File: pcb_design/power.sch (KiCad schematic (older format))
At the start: 35 parts, among them Q1 BSC340N08, U11 LM3488, U13 LM1117IMP-v.v, U9 LM22676QTJ-5.0

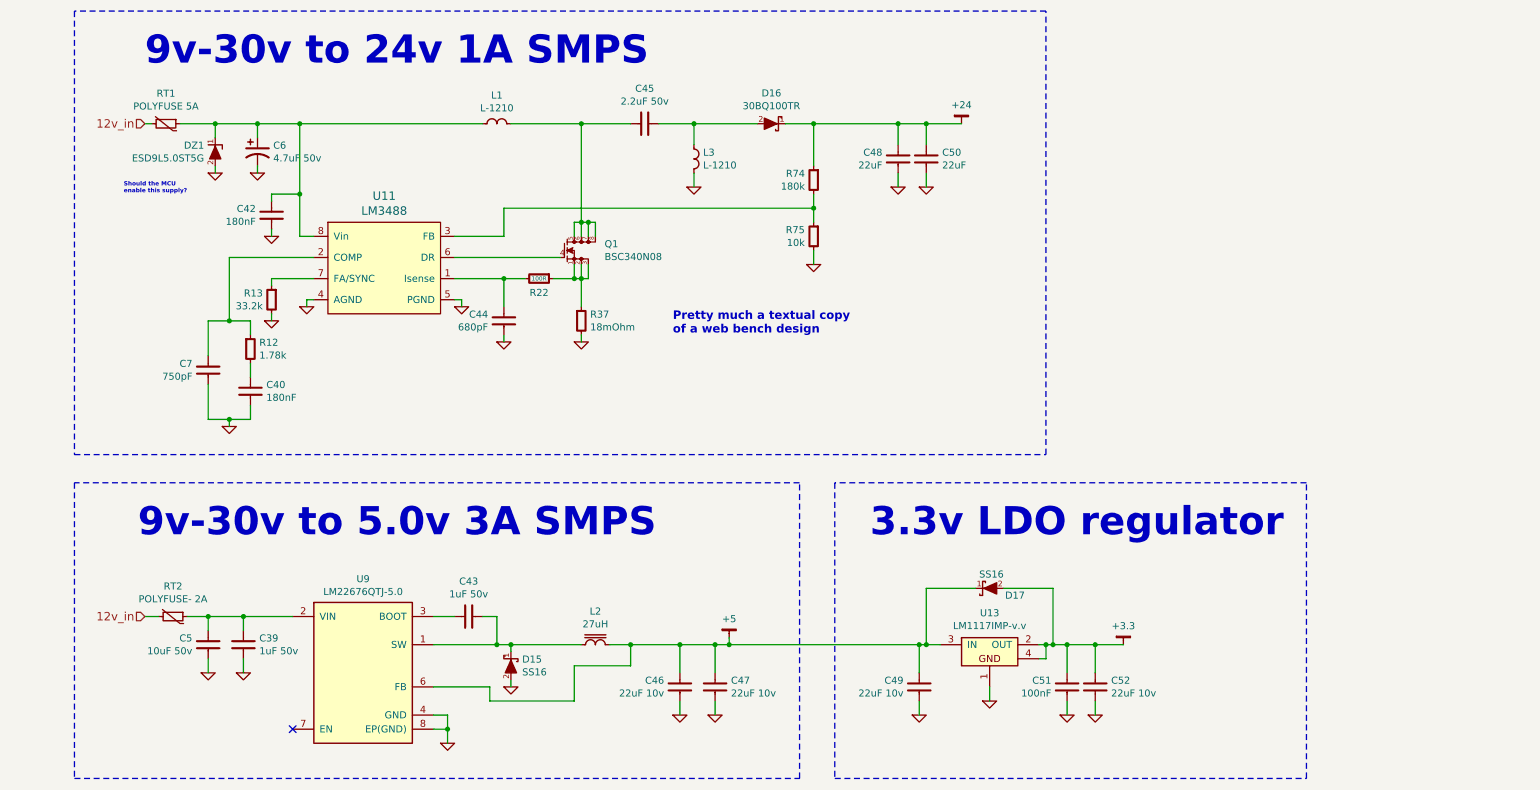
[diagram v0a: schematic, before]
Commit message: Resolver routed using push pull buffer
Signed-off-by: Marcos Chaparro <mchaparro@paltatech.com>
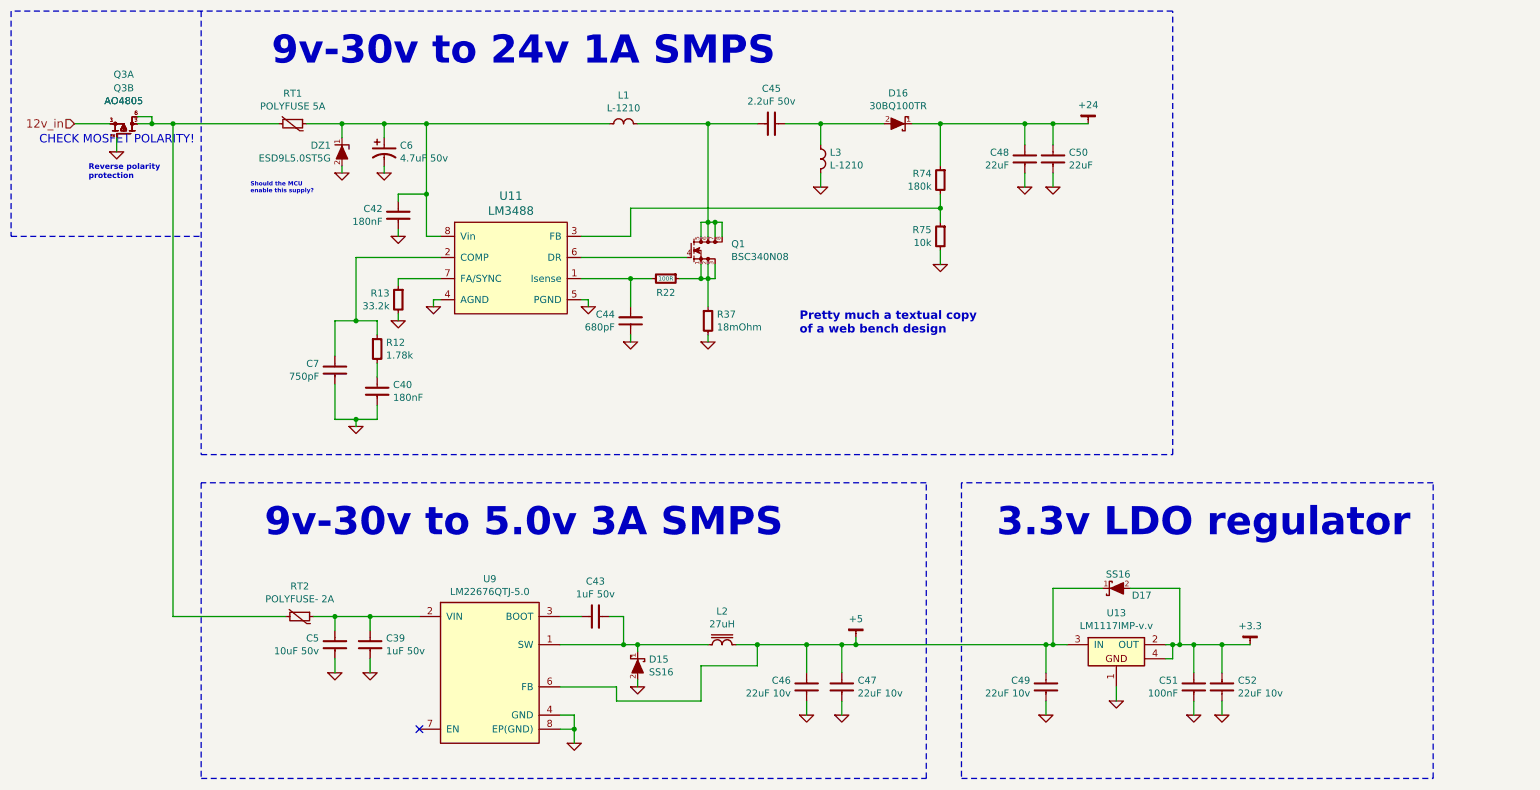
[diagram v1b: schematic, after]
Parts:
- added Q3: AO4805, IPC7351-Nominal:SOIC127P600X175-8, symbol AO4805
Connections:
- net 12v_in: now also Q3.1 (S2), Q3.3 (S1); no longer RT1.2, RT2.2
- net GND: now also Q3.2 (G1), Q3.4 (G1)
- new net: Q3.5 (D1A), Q3.6 (D1B), Q3.7 (D2A), Q3.8 (D2B), RT1.2, RT2.2
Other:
- note added: "CHECK MOSFET POLARITY!"
- note added: "Reverse polarity\nprotection"
- moved on the sheet: C39, C40, C42, C43, C44, C45, C46, C47, C48, C49, C5, C50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

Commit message: Routing complete. Added 3D models. No DRC errors, a few ERC warnings
Signed-off-by: Marcos Chaparro <mchaparro@paltatech.com>
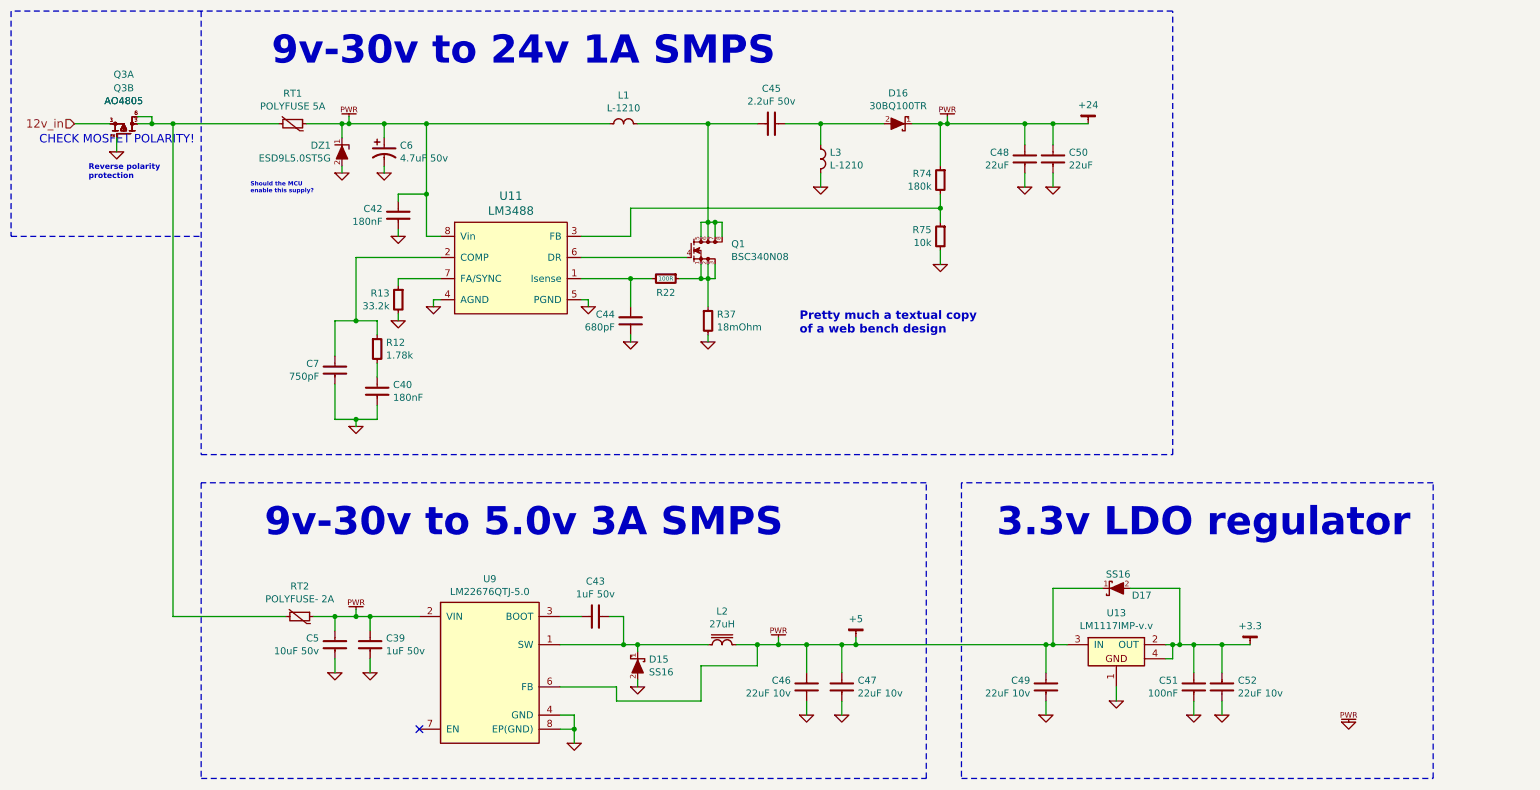
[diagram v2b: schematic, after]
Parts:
- L2: footprint manuf:BOURNS-SRP1238A -> manuf:BOURNS-SDR1307
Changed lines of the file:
@@
 Connection ~ 3000 4150
 $Comp
-L GND #PWR067
+L GND #PWR073
 U 1 1 588BC982
 P 3000 4200
-F 0 "#PWR067" H 3000 4200 30  0001 C CNN
+F 0 "#PWR073" H 3000 4200 30  0001 C CNN
 F 1 "GND" H 3000 4130 30  0001 C CNN
 F 2 "" H 3000 4200 60  0000 C CNN
@@
 	3300 3150 3300 3200
 $Comp
-L GND #PWR068
+L GND #PWR074
 U 1 1 588BD2D9
 P 3300 3450
-F 0 "#PWR068" H 3300 3450 30  0001 C CNN
+F 0 "#PWR074" H 3300 3450 30  0001 C CNN
 F 1 "GND" H 3300 3380 30  0001 C CNN
 F 2 "" H 3300 3450 60  0000 C CNN
@@
 	3300 3450 3300 3400
 $Comp
-L GND #PWR069
+L GND #PWR075
 U 1 1 588BD345
 P 3550 3350
-F 0 "#PWR069" H 3550 3350 30  0001 C CNN
+F 0 "#PWR075" H 3550 3350 30  0001 C CNN
 F 1 "GND" H 3550 3280 30  0001 C CNN
 F 2 "" H 3550 3350 60  0000 C CNN
@@
 	4650 3300 4650 3350
 $Comp
-L GND #PWR070
+L GND #PWR076
 U 1 1 588BD634
 P 4650 3350
-F 0 "#PWR070" H 4650 3350 30  0001 C CNN
+F 0 "#PWR076" H 4650 3350 30  0001 C CNN
 F 1 "GND" H 4650 3280 30  0001 C CNN
 F 2 "" H 4650 3350 60  0000 C CNN
@@
 	4950 3550 4950 3600
 $Comp
-L GND #PWR071
+L GND #PWR077
 U 1 1 588BDA1B
 P 4950 3600
-F 0 "#PWR071" H 4950 3600 30  0001 C CNN
+F 0 "#PWR077" H 4950 3600 30  0001 C CNN
 F 1 "GND" H 4950 3530 30  0001 C CNN
 F 2 "" H 4950 3600 60  0000 C CNN
@@
 	5500 3550 5500 3600
 $Comp
-L GND #PWR072
+L GND #PWR078
 U 1 1 588BDE06
 P 5500 3600
-F 0 "#PWR072" H 5500 3600 30  0001 C CNN
+F 0 "#PWR078" H 5500 3600 30  0001 C CNN
 F 1 "GND" H 5500 3530 30  0001 C CNN
 F 2 "" H 5500 3600 60  0000 C CNN
@@
 Connection ~ 3500 2550
 $Comp
-L GND #PWR073
+L GND #PWR079
 U 1 1 588BFA6D
 P 3300 2850
-F 0 "#PWR073" H 3300 2850 30  0001 C CNN
+F 0 "#PWR079" H 3300 2850 30  0001 C CNN
 F 1 "GND" H 3300 2780 30  0001 C CNN
 F 2 "" H 3300 2850 60  0000 C CNN
@@
 	3200 2150 3200 2050
 $Comp
-L GND #PWR074
+L GND #PWR080
 U 1 1 588C0261
 P 3200 2400
-F 0 "#PWR074" H 3200 2400 30  0001 C CNN
+F 0 "#PWR080" H 3200 2400 30  0001 C CNN
 F 1 "GND" H 3200 2330 30  0001 C CNN
 F 2 "" H 3200 2400 60  0000 C CNN
@@
 	6050 2050 6750 2050
 $Comp
-L GND #PWR075
+L GND #PWR081
 U 1 1 588C0D64
 P 6300 2500
-F 0 "#PWR075" H 6300 2500 30  0001 C CNN
+F 0 "#PWR081" H 6300 2500 30  0001 C CNN
 F 1 "GND" H 6300 2430 30  0001 C CNN
 F 2 "" H 6300 2500 60  0000 C CNN
@@
 	6950 2050 8200 2050
 $Comp
-L GND #PWR076
+L GND #PWR082
 U 1 1 588C18FD
 P 7150 3050
-F 0 "#PWR076" H 7150 3050 30  0001 C CNN
+F 0 "#PWR082" H 7150 3050 30  0001 C CNN
 F 1 "GND" H 7150 2980 30  0001 C CNN
 F 2 "" H 7150 3050 60  0000 C CNN
@@
 Connection ~ 7750 2050
 $Comp
-L GND #PWR077
+L GND #PWR083
 U 1 1 588C2312
 P 7750 2500
-F 0 "#PWR077" H 7750 2500 30  0001 C CNN
+F 0 "#PWR083" H 7750 2500 30  0001 C CNN
 F 1 "GND" H 7750 2430 30  0001 C CNN
 F 2 "" H 7750 2500 60  0000 C CNN
@@
 	7750 2500 7750 2400
 $Comp
-L GND #PWR078
+L GND #PWR084
 U 1 1 588C2433
 P 7950 2500
-F 0 "#PWR078" H 7950 2500 30  0001 C CNN
+F 0 "#PWR084" H 7950 2500 30  0001 C CNN
 F 1 "GND" H 7950 2430 30  0001 C CNN
 F 2 "" H 7950 2500 60  0000 C CNN
@@
 Connection ~ 3100 5550
 $Comp
-L GND #PWR079
+L GND #PWR085
 U 1 1 588C4382
 P 2850 5950
-F 0 "#PWR079" H 2850 5950 30  0001 C CNN
+F 0 "#PWR085" H 2850 5950 30  0001 C CNN
 F 1 "GND" H 2850 5880 30  0001 C CNN
 F 2 "" H 2850 5950 60  0000 C CNN
@@
 	2850 5950 2850 5850
 $Comp
-L GND #PWR080
+L GND #PWR086
 U 1 1 588C4468
 P 3100 5950
-F 0 "#PWR080" H 3100 5950 30  0001 C CNN
+F 0 "#PWR086" H 3100 5950 30  0001 C CNN
 F 1 "GND" H 3100 5880 30  0001 C CNN
 F 2 "" H 3100 5950 60  0000 C CNN
@@
 Connection ~ 4900 5750
 $Comp
-L GND #PWR081
+L GND #PWR087
 U 1 1 588C56F7
 P 5000 6050
-F 0 "#PWR081" H 5000 6050 30  0001 C CNN
+F 0 "#PWR087" H 5000 6050 30  0001 C CNN
 F 1 "GND" H 5000 5980 30  0001 C CNN
 F 2 "" H 5000 6050 60  0000 C CNN
@@
 F 0 "L2" V 5363 5750 50  0000 C CNN
 F 1 "27uH" V 5454 5750 50  0000 C CNN
-F 2 "manuf:BOURNS-SRP1238A" H 5600 5800 60  0001 C CNN
+F 2 "manuf:BOURNS-SDR1307" H 5600 5800 60  0001 C CNN
 F 3 "" H 5600 5800 60  0000 C CNN
 F 4 "SDR1307-270ML" H 5600 5750 60  0001 C CNN "mfg#"
@@
 Connection ~ 6200 5750
 $Comp
-L GND #PWR082
+L GND #PWR088
 U 1 1 588C63EB
 P 6200 6250
-F 0 "#PWR082" H 6200 6250 30  0001 C CNN
+F 0 "#PWR088" H 6200 6250 30  0001 C CNN
 F 1 "GND" H 6200 6180 30  0001 C CNN
 F 2 "" H 6200 6250 60  0000 C CNN
@@
 $EndComp
 $Comp
-L GND #PWR083
+L GND #PWR089
 U 1 1 588C6447
 P 6450 6250
-F 0 "#PWR083" H 6450 6250 30  0001 C CNN
+F 0 "#PWR089" H 6450 6250 30  0001 C CNN
 F 1 "GND" H 6450 6180 30  0001 C CNN
 F 2 "" H 6450 6250 60  0000 C CNN
@@
 NoConn ~ 3450 6350
 $Comp
-L GND #PWR084
+L GND #PWR090
 U 1 1 588C6DC2
 P 4550 6450
-F 0 "#PWR084" H 4550 6450 30  0001 C CNN
+F 0 "#PWR090" H 4550 6450 30  0001 C CNN
 F 1 "GND" H 4550 6380 30  0001 C CNN
 F 2 "" H 4550 6450 60  0000 C CNN
@@
 Connection ~ 7900 5750
 $Comp
-L GND #PWR085
+L GND #PWR091
 U 1 1 588C792B
 P 7900 6250
-F 0 "#PWR085" H 7900 6250 30  0001 C CNN
+F 0 "#PWR091" H 7900 6250 30  0001 C CNN
 F 1 "GND" H 7900 6180 30  0001 C CNN
 F 2 "" H 7900 6250 60  0000 C CNN
@@
 	7900 6250 7900 6150
 $Comp
-L GND #PWR086
+L GND #PWR092
 U 1 1 588C79EC
 P 8400 6150
-F 0 "#PWR086" H 8400 6150 30  0001 C CNN
+F 0 "#PWR092" H 8400 6150 30  0001 C CNN
 F 1 "GND" H 8400 6080 30  0001 C CNN
 F 2 "" H 8400 6150 60  0000 C CNN
@@
 Connection ~ 8950 5750
 $Comp
-L GND #PWR087
+L GND #PWR093
 U 1 1 588C813C
 P 8950 6250
-F 0 "#PWR087" H 8950 6250 30  0001 C CNN
+F 0 "#PWR093" H 8950 6250 30  0001 C CNN
 F 1 "GND" H 8950 6180 30  0001 C CNN
 F 2 "" H 8950 6250 60  0000 C CNN
@@
 	8950 6250 8950 6150
 $Comp
-L GND #PWR088
+L GND #PWR094
 U 1 1 588C81BF
 P 9150 6250
-F 0 "#PWR088" H 9150 6250 30  0001 C CNN
+F 0 "#PWR094" H 9150 6250 30  0001 C CNN
 F 1 "GND" H 9150 6180 30  0001 C CNN
 F 2 "" H 9150 6250 60  0000 C CNN
@@
 	10650 4600 7300 4600
 $Comp
-L +3.3 #PWR089
+L +3.3 #PWR095
 U 1 1 588BD2B2
 P 9350 5750
-F 0 "#PWR089" H 9400 5800 30  0001 C CNN
+F 0 "#PWR095" H 9400 5800 30  0001 C CNN
 F 1 "+3.3" H 9350 5883 50  0000 C CNN
 F 2 "" H 800 0   60  0000 C CNN
@@
 $EndComp
 $Comp
-L +5 #PWR090
+L +5 #PWR096
 U 1 1 588BD705
 P 6550 5700
-F 0 "#PWR090" H 6600 5750 30  0001 C CNN
+F 0 "#PWR096" H 6600 5750 30  0001 C CNN
 F 1 "+5" H 6550 5833 50  0000 C CNN
 F 2 "" H 500 50  60  0000 C CNN
@@
 Connection ~ 2900 2050
 $Comp
-L GND #PWR091
+L GND #PWR097
 U 1 1 588CB9A0
 P 2900 2400
-F 0 "#PWR091" H 2900 2400 30  0001 C CNN
+F 0 "#PWR097" H 2900 2400 30  0001 C CNN
 F 1 "GND" H 2900 2330 30  0001 C CNN
 F 2 "" H 2900 2400 60  0000 C CNN
@@
 Connection ~ 7950 5750
 $Comp
-L +24 #PWR092
+L +24 #PWR098
 U 1 1 588CFB19
 P 8200 2050
-F 0 "#PWR092" H 800 50  30  0001 C CNN
+F 0 "#PWR098" H 800 50  30  0001 C CNN
 F 1 "+24" H 8200 2183 50  0000 C CNN
 F 2 "" H 800 0   60  0000 C CNN
@@
 Connection ~ 1550 2050
 $Comp
-L GND #PWR093
+L GND #PWR099
 U 1 1 588F9181
 P 1300 2250
-F 0 "#PWR093" H 1300 2250 30  0001 C CNN
+F 0 "#PWR099" H 1300 2250 30  0001 C CNN
 F 1 "GND" H 1300 2180 30  0001 C CNN
 F 2 "" H 1300 2250 60  0000 C CNN
@@
 Text Notes 750  2200 0    60   ~ 0
 CHECK MOSFET POLARITY!
+$Comp
+L PWR_FLAG #PWR0100
+U 1 1 58939EB5
+P 6000 5700
+F 0 "#PWR0100" H 6050 5750 50  0001 C CNN
+F 1 "PWR_FLAG" H -3050 3650 50  0001 C CNN
+F 2 "" H -3050 3650 60  0000 C CNN
+F 3 "" H -3050 3650 60  0000 C CNN
+	1    6000 5700
+	1    0    0    -1
+$EndComp
+Wire Wire Line
+	6000 5700 6000 5750
+Connection ~ 6000 5750
+$Comp
+L PWR_FLAG #PWR0101
+U 1 1 5893A517
+P 7200 2000
+F 0 "#PWR0101" H 7250 2050 50  0001 C CNN
+F 1 "PWR_FLAG" H -1850 -50 50  0001 C CNN
+F 2 "" H -1850 -50 60  0000 C CNN
+F 3 "" H -1850 -50 60  0000 C CNN
+	1    7200 2000
+	1    0    0    -1
+$EndComp
+Wire Wire Line
+	7200 2000 7200 2050
+Connection ~ 7200 2050
+$Comp
+L PWR_FLAG #PWR0102
+U 1 1 5894047A
+P 3000 5500
+F 0 "#PWR0102" H 50  150 50  0001 C CNN
+F 1 "PWR_FLAG" H 50  150 50  0001 C CNN
+F 2 "" H 50  150 60  0000 C CNN
+F 3 "" H 50  150 60  0000 C CNN
+	1    3000 5500
+	1    0    0    -1
+$EndComp
+Wire Wire Line
+	3000 5500 3000 5550
+Connection ~ 3000 5550
+$Comp
+L PWR_FLAG #PWR0103
+U 1 1 589407AF
+P 2950 2000
+F 0 "#PWR0103" H -550 50  50  0001 C CNN
+F 1 "PWR_FLAG" H -550 50  50  0001 C CNN
+F 2 "" H -550 50  60  0000 C CNN
+F 3 "" H -550 50  60  0000 C CNN
+	1    2950 2000
+	1    0    0    -1
+$EndComp
+Wire Wire Line
+	2950 2000 2950 2050
+Connection ~ 2950 2050
+$Comp
+L PWR_FLAG #PWR0104
+U 1 1 58945B82
+P 10050 6300
+F 0 "#PWR0104" H 10100 6350 50  0001 C CNN
+F 1 "PWR_FLAG" H -200 -200 50  0001 C CNN
+F 2 "" H -200 -200 60  0000 C CNN
+F 3 "" H -200 -200 60  0000 C CNN
+	1    10050 6300
+	1    0    0    -1
+$EndComp
+$Comp
+L GND #PWR0105
+U 1 1 58945C4D
+P 10050 6300
+F 0 "#PWR0105" H 10050 6300 30  0001 C CNN
+F 1 "GND" H 10050 6230 30  0001 C CNN
+F 2 "" H 10050 6300 60  0000 C CNN
+F 3 "" H 10050 6300 60  0000 C CNN
+	1    10050 6300
+	1    0    0    -1
+$EndComp
 $EndSCHEMATC

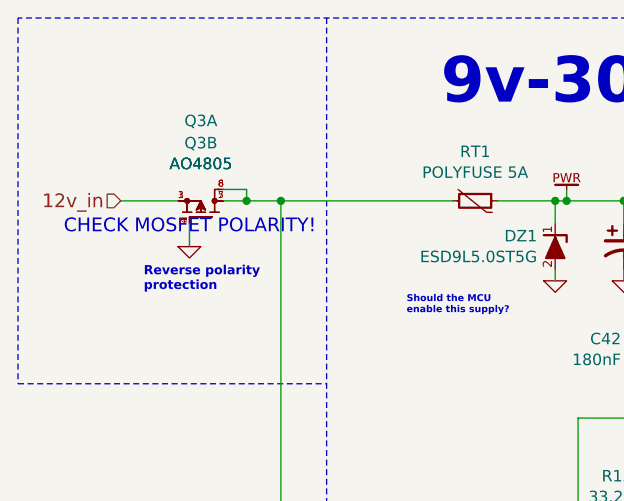
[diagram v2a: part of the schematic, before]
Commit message: Added frequency set resistors for the resolver. Fixed protection mosfet installed backwards. More 3D models
Signed-off-by: Marcos Chaparro <mchaparro@paltatech.com>
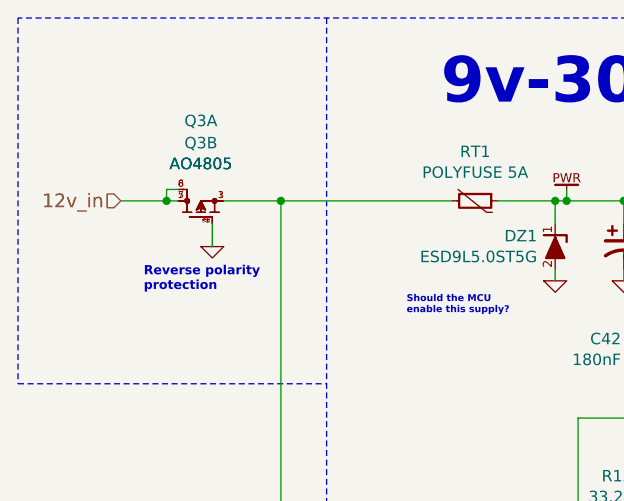
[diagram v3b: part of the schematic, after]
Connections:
- net 12v_in: now also Q3.5 (D1A), Q3.6 (D1B), Q3.7 (D2A), Q3.8 (D2B); no longer Q3.1 (S2), Q3.3 (S1)
- new net: Q3.1 (S2), Q3.3 (S1), RT1.2, RT2.2
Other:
- note removed: "CHECK MOSFET POLARITY!"
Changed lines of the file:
@@
 F 4 "PMOS AOS AO4805" H -1500 -2850 60  0001 C CNN "BOM"
 	1    1350 2100
-	0    -1   -1   0
+	0    1    -1   0
 $EndComp
 Wire Wire Line
 	1000 2050 1250 2050
-Wire Wire Line
-	1450 2000 1550 2000
-Wire Wire Line
-	1550 2000 1550 2050
-Connection ~ 1550 2050
 $Comp
 L GND #PWR099
 U 1 1 588F9181
-P 1300 2250
-F 0 "#PWR099" H 1300 2250 30  0001 C CNN
-F 1 "GND" H 1300 2180 30  0001 C CNN
-F 2 "" H 1300 2250 60  0000 C CNN
-F 3 "" H 1300 2250 60  0000 C CNN
-	1    1300 2250
+P 1400 2250
+F 0 "#PWR099" H 1400 2250 30  0001 C CNN
+F 1 "GND" H 1400 2180 30  0001 C CNN
+F 2 "" H 1400 2250 60  0000 C CNN
+F 3 "" H 1400 2250 60  0000 C CNN
+	1    1400 2250
 	1    0    0    -1
 $EndComp
 Wire Wire Line
-	1300 2250 1300 2150
+	1400 2250 1400 2150
 Wire Wire Line
 	1700 2050 1700 5550
@@
 F 4 "PMOS AOS AO4805" H -1500 -2850 60  0001 C CNN "BOM"
 	2    1350 2100
-	0    -1   -1   0
+	0    1    -1   0
 $EndComp
-Text Notes 750  2200 0    60   ~ 0
-CHECK MOSFET POLARITY!
 $Comp
 L PWR_FLAG #PWR0100
@@
 	1    0    0    -1
 $EndComp
+Wire Wire Line
+	1250 2000 1200 2000
+Wire Wire Line
+	1200 2000 1200 2050
+Connection ~ 1200 2050
 $EndSCHEMATC

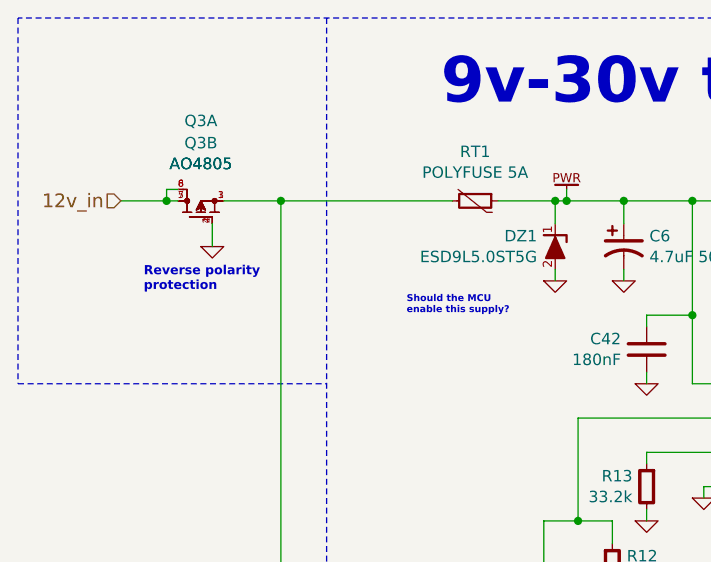
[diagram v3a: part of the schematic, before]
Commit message: Silkscreen logos, fixed swapped OCP inputs, added a button to enter bootloader,missing 3d model.
Signed-off-by: Marcos Chaparro <mchaparro@paltatech.com>
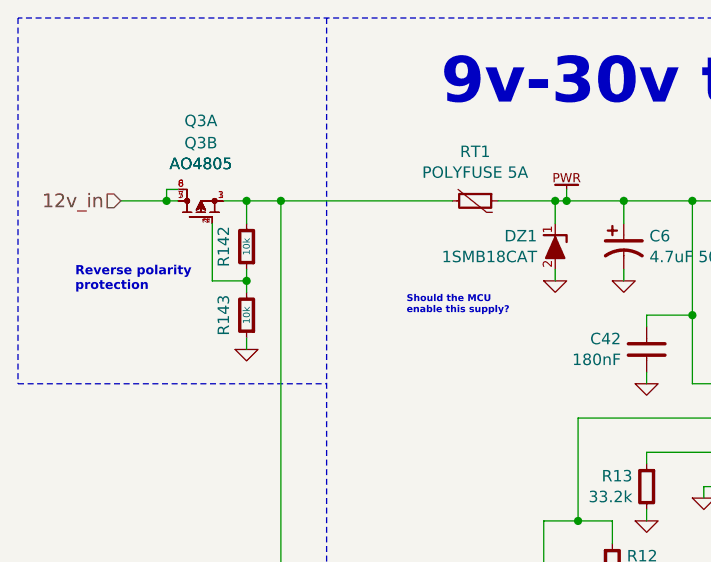
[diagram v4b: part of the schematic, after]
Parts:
- added R142, R143: 10k, IPC7351-Nominal:RESC1608X50, symbol R-0603
- DZ1: value ESD9L5.0ST5G -> 1SMB18CAT; footprint smd-semi:SOD-THAT -> w_smd_diode:do214aa; BOM TVS ONSEMI ESD9L5.0ST5G -> TVS ONSEMI 1SMB18CAT; mfg# (none) -> 1SMB18CAT3GOSCT-ND
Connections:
- net GND: now also R143.1; no longer Q3.2 (G1), Q3.4 (G1)
- net at Q3.1 (S2), Q3.3 (S1), RT1.2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: now also R142.2
- new net: Q3.2 (G1), Q3.4 (G1), R142.1, R143.2
